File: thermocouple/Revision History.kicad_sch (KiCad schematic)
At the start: 0 parts

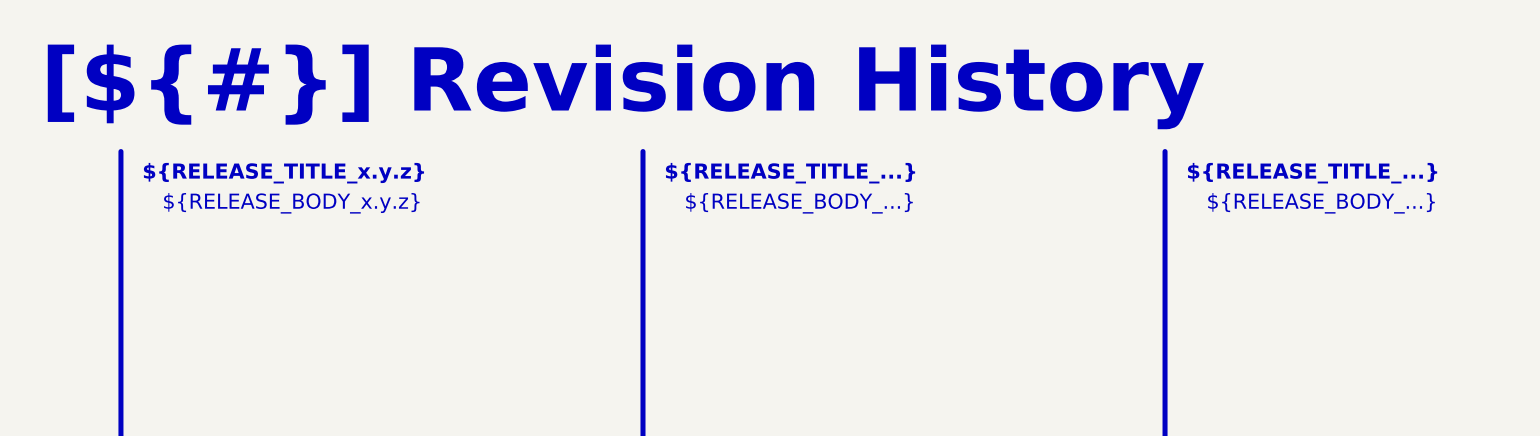
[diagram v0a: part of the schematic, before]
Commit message: CI/CD improvements, fixing broken PMIC-INT
- Update CI/CD to the latest version
- Move PMIC-INT to port 0 to make it usable

Signed-off-by: Daniel Kampert <DanielKampert@kampis-elektroecke.de>
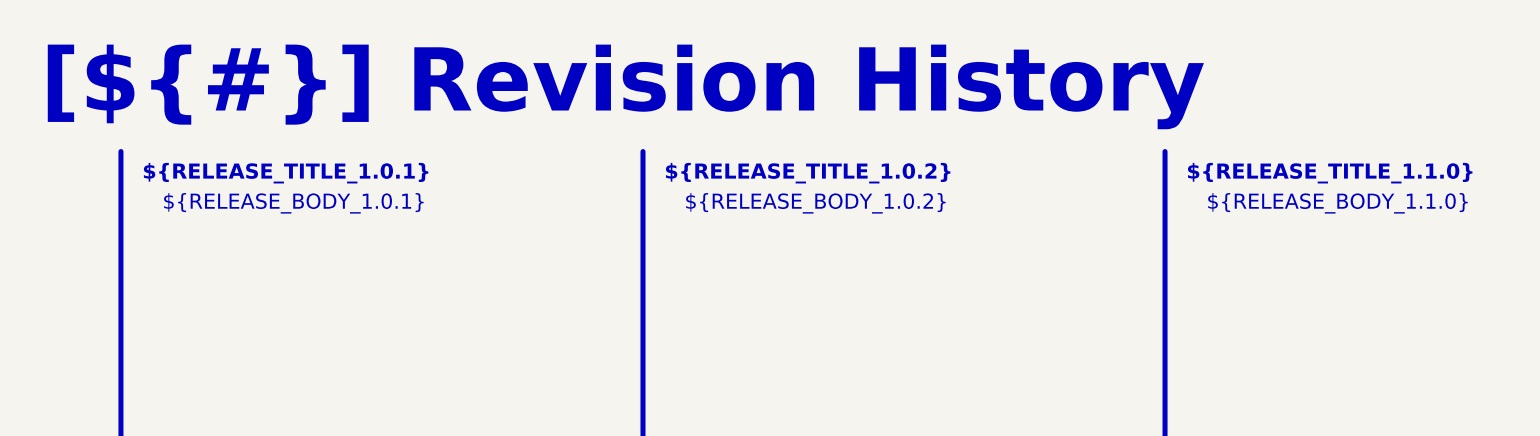
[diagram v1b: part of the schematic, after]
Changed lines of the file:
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@@
 		(company "${COMPANY}")
 	)
-	(text_box "${RELEASE_BODY_...}"
+	(text_box "${RELEASE_BODY_1.1.0}"
 		(exclude_from_sim no)
 		(at 220.98 35.56 0)
@@
 		)
 	)
-	(text_box "${RELEASE_TITLE_...}"
+	(text_box "${RELEASE_TITLE_1.0.2}"
 		(exclude_from_sim no)
 		(at 152.4 31.75 0)
@@
 		)
 	)
-	(text_box "${RELEASE_BODY_...}"
+	(text_box "${RELEASE_BODY_1.0.2}"
 		(exclude_from_sim no)
 		(at 154.94 35.56 0)
@@
 		)
 	)
-	(text_box "${RELEASE_BODY_x.y.z}"
+	(text_box "${RELEASE_BODY_1.0.1}"
 		(exclude_from_sim no)
 		(at 88.9 35.56 0)
@@
 		)
 	)
-	(text_box "${RELEASE_TITLE_x.y.z}"
+	(text_box "${RELEASE_TITLE_1.0.1}"
 		(exclude_from_sim no)
 		(at 86.36 31.75 0)
@@
 		)
 	)
-	(text_box "${RELEASE_TITLE_...}"
+	(text_box "${RELEASE_TITLE_1.1.0}"
 		(exclude_from_sim no)
 		(at 218.44 31.75 0)
